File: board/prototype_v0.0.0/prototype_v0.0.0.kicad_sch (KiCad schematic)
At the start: 5 parts, among them U1 ATmega328PB-A, Y1 16MHz

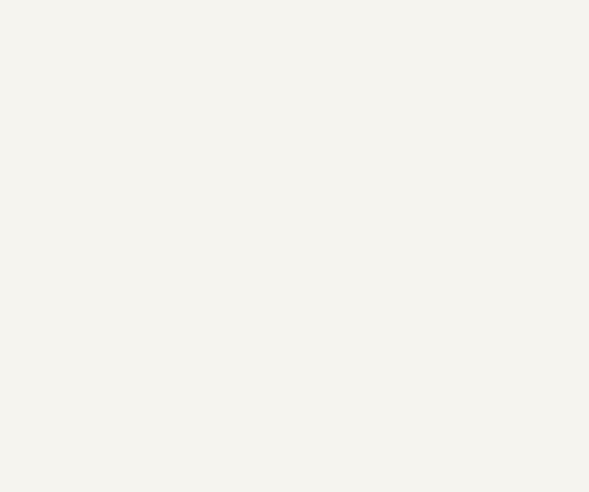
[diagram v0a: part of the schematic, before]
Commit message: BRD-2025 added CH340C
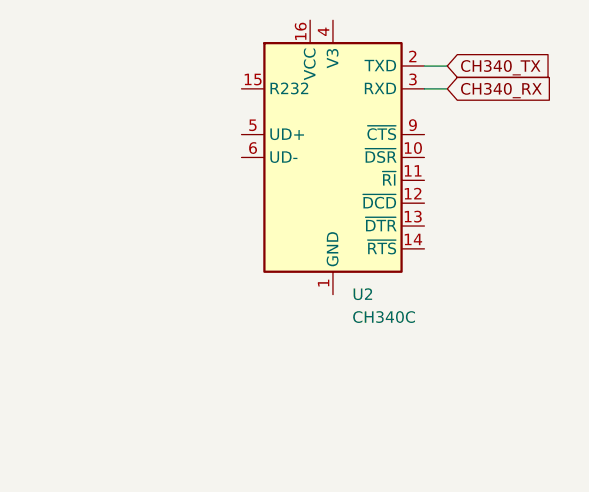
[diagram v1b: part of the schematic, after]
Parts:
- added U2: CH340C, Package_SO:SOIC-16_3.9x9.9mm_P1.27mm, symbol Interface_USB:CH340C
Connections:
- net CH340_RX: now also U2.3 (RXD)
- net CH340_TX: now also U2.2 (TXD)
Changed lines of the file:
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@@
+	(wire
+		(pts
+			(xy 261.62 53.34) (xy 259.08 53.34)
+		)
+		(stroke
+			(width 0)
+			(type default)
+		)
+	)
 	(wire
 		(pts
@@
 		(pts
 			(xy 165.1 78.74) (xy 165.1 80.01)
+		)
+		(stroke
+			(width 0)
+			(type default)
+		)
+	)
+	(wire
+		(pts
+			(xy 261.62 55.88) (xy 259.08 55.88)
 		)
 		(stroke
@@
 		)
 	)
+	(global_label "CH340_TX"
+		(shape input)
+		(at 261.62 53.34 0)
+		(fields_autoplaced yes)
+		(effects
+			(font
+				(size 1.27 1.27)
+			)
+			(justify left)
+		)
+		(property "Intersheetrefs" "${INTERSHEET_REFS}"
+			(at 273.9789 53.34 0)
+			(effects
+				(font
+					(size 1.27 1.27)
+				)
+				(justify left)
+				(hide yes)
+			)
+		)
+	)
 	(global_label "CH340_RX"
 		(shape input)
@@
 		(property "Intersheetrefs" "${INTERSHEET_REFS}"
 			(at 170.1413 101.6 0)
+			(effects
+				(font
+					(size 1.27 1.27)
+				)
+				(justify left)
+				(hide yes)
+			)
+		)
+	)
+	(global_label "CH340_RX"
+		(shape input)
+		(at 261.62 55.88 0)
+		(fields_autoplaced yes)
+		(effects
+			(font
+				(size 1.27 1.27)
+			)
+			(justify left)
+		)
+		(property "Intersheetrefs" "${INTERSHEET_REFS}"
+			(at 274.2813 55.88 0)
 			(effects
 				(font
@@
 					(unit 1)
 				)
+			)
+		)
+	)
+	(symbol
+		(lib_id "Interface_USB:CH340C")
+		(at 248.92 63.5 0)
+		(unit 1)
+		(exclude_from_sim no)
+		(in_bom yes)
+		(on_board yes)
+		(dnp no)
+		(fields_autoplaced yes)
+		(property "Reference" "U2"
+			(at 251.0633 78.74 0)
+			(effects
+				(font
+					(size 1.27 1.27)
+				)
+				(justify left)
+			)
+		)
+		(property "Value" "CH340C"
+			(at 251.0633 81.28 0)
+			(effects
+				(font
+					(size 1.27 1.27)
+				)
+				(justify left)
+			)
+		)
+		(property "Footprint" "Package_SO:SOIC-16_3.9x9.9mm_P1.27mm"
+			(at 230.378 33.274 0)
+			(effects
+				(font
+					(size 1.27 1.27)
+				)
+				(justify left)
+				(hide yes)
+			)
+		)
+		(property "Datasheet" "https://datasheet.lcsc.com/szlcsc/Jiangsu-Qin-Heng-CH340C_C84681.pdf"
+			(at 242.316 30.226 0)
+			(effects
+				(font
+					(size 1.27 1.27)
+				)
+				(hide yes)
+			)
+		)
+		(property "Description" "USB serial converter, crystal-less, UART, SOIC-16"
+			(at 247.396 27.432 0)
+			(effects
+				(font
+					(size 1.27 1.27)
+				)
+				(hide yes)
+			)
+		)
+		(pin "14"
+		)
+		(pin "10"
+		)
+		(pin "13"
+		)
+		(pin "4"
+		)
+		(pin "1"
+		)
+		(pin "7"
+		)
+		(pin "16"
+		)
+		(pin "11"
+		)
+		(pin "5"
+		)
+		(pin "6"
+		)
+		(pin "15"
+		)
+		(pin "8"
+		)
+		(pin "2"
+		)
+		(pin "12"
+		)
+		(pin "3"
+		)
+		(pin "9"
+		)
+		(instances
+			(project ""
+				(path "/f997ee1a-6397-42e7-9ccf-5171b4489c6c"
+					(reference "U2")
+					(unit 1)
+				)

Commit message: BRD schematic update
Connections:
- net DTR: now also U2.13 (~{DTR})
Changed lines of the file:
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@@
+	(wire
+		(pts
+			(xy 259.08 71.12) (xy 261.62 71.12)
+		)
+		(stroke
+			(width 0)
+			(type default)
+		)
+	)
 	(wire
 		(pts
@@
 			(effects
 				(font
+					(size 1.27 1.27)
+				)
+				(justify left)
+				(hide yes)
+			)
+		)
+	)
+	(global_label "DTR"
+		(shape input)
+		(at 261.62 71.12 0)
+		(fields_autoplaced yes)
+		(effects
+			(font
+				(size 1.27 1.27)
+			)
+			(justify left)
+		)
+		(property "Intersheetrefs" "${INTERSHEET_REFS}"
+			(at 268.1128 71.12 0)
+			(effects
+				(font

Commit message: BRD schematic update
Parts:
- added D1, D2: LED, symbol Device:LED
- added R1, R2: 1k, symbol Device:R_Small
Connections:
- net CH340_RX: now also D2.1 (K)
- net CH340_TX: now also D1.1 (K)
- new net: D2.2 (A), R1.2
- new net: D1.2 (A), R2.2
- new net +3.3V: R1.1, R2.1
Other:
- moved on the sheet: C1, C2, C3, U1, U2, Y1
